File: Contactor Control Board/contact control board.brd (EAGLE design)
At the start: 57.1 x 50.8 mm, 35 parts, among them Q1 MMBT2222A, Q2 MMBT2222A, Q3 IRLML6344TRPBF, Q6 IRLML6344TRPBF

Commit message: Routed BMS interface board and added branding.
Changed branding for CCB and MCBs
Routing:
- net CONTACT_EN: track 91.4 -> 90.1 mm
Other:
- board text added: "Prosthesis CCB V1.0"
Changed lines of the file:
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@@
 <text x="25.7175" y="6.6675" size="1.016" layer="25" font="vector" ratio="15">+ve</text>
 <text x="13.6525" y="6.6675" size="1.016" layer="25" font="vector" ratio="15">+ve</text>
+<text x="40.64" y="13.0175" size="1.778" layer="25" font="vector" ratio="15">Prosthesis
+CCB V1.0</text>
 </plain>
 <attributes>
@@
 <wire x1="20.32" y1="1.905" x2="50.4825" y2="1.905" width="0.3048" layer="1"/>
 <wire x1="50.4825" y1="1.905" x2="51.1175" y2="2.54" width="0.3048" layer="1"/>
-<wire x1="51.1175" y1="2.54" x2="51.1175" y2="13.335" width="0.3048" layer="1"/>
-<wire x1="51.1175" y1="13.335" x2="51.435" y2="13.6525" width="0.3048" layer="1"/>
-<via x="51.435" y="13.6525" extent="1-16" drill="0.508"/>
-<wire x1="51.435" y1="13.6525" x2="53.6575" y2="13.6525" width="0.3048" layer="16"/>
+<wire x1="51.1175" y1="2.54" x2="51.1175" y2="11.1125" width="0.3048" layer="1"/>
+<wire x1="51.1175" y1="11.1125" x2="53.6575" y2="13.6525" width="0.3048" layer="1"/>
+<via x="53.6575" y="13.6525" extent="1-16" drill="0.762"/>
 <wire x1="53.6575" y1="13.6525" x2="54.61" y2="14.605" width="0.3048" layer="16"/>
 <wire x1="54.61" y1="14.605" x2="54.61" y2="21.2725" width="0.3048" layer="16"/>

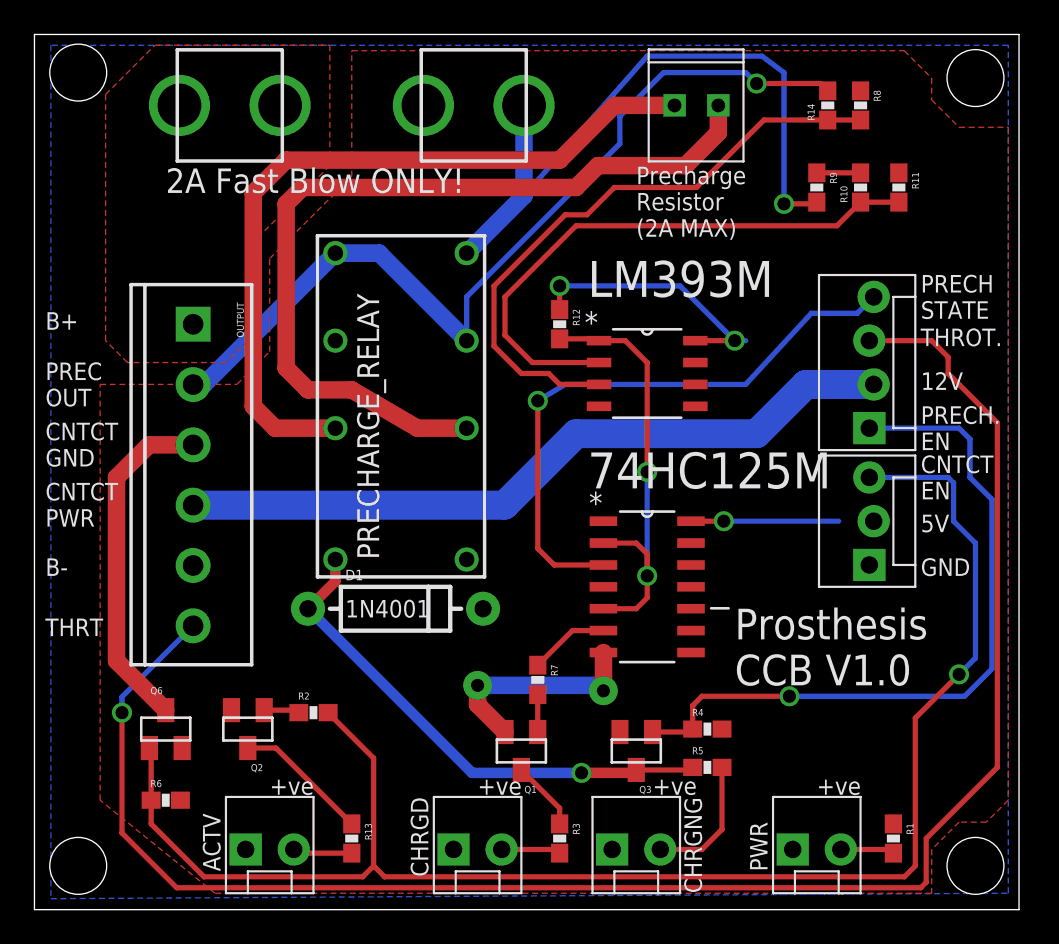
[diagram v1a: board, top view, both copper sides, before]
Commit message: UPdating resistor packages to sizes which are
capable of disappating the appropriate amount of power.
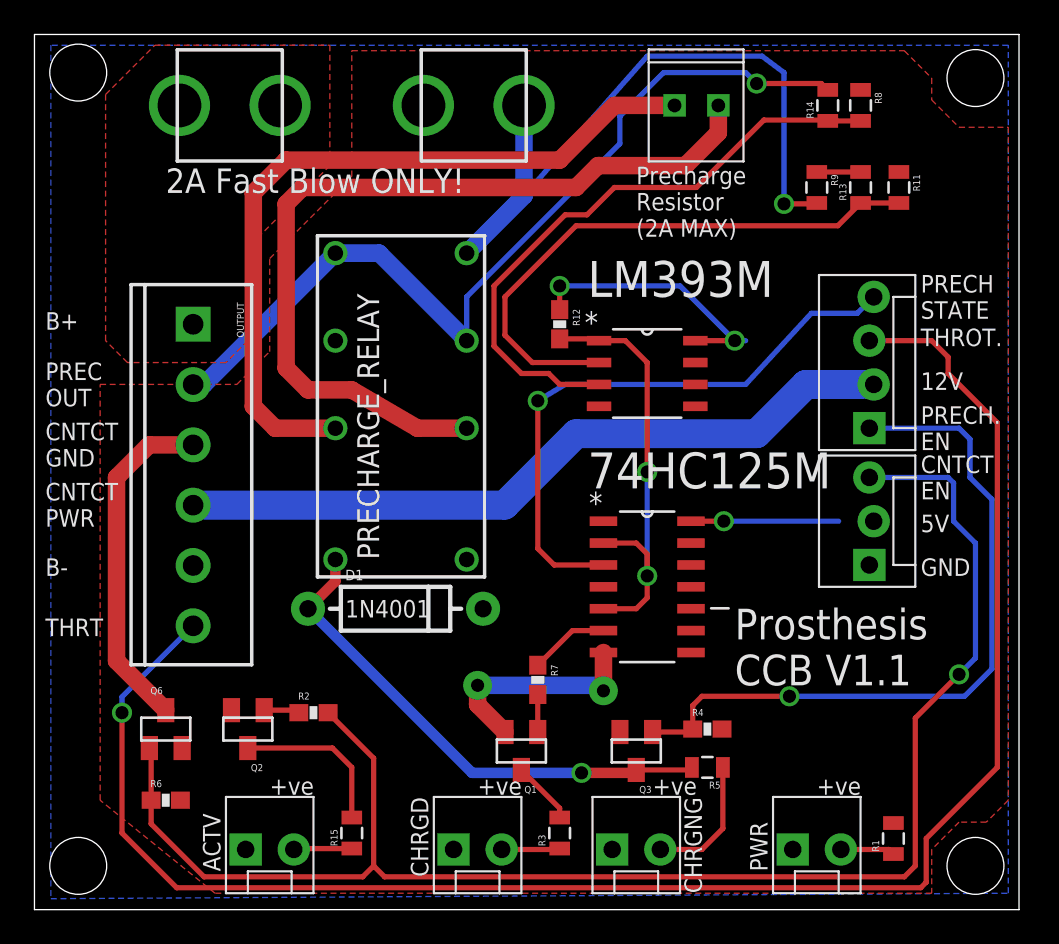
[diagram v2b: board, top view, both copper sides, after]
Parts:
- removed R10: 110k, SparkFun-Resistors:0603-RES
- added R15: 470, SparkFun-Resistors:0805
- R1, R14, R3, R5, R9: device SparkFun-Resistors:0603-RES -> SparkFun-Resistors:0805
- R11: value 12k -> 12K; device SparkFun-Resistors:0603-RES -> SparkFun-Resistors:0805
- R13: value 470 -> 110k; device SparkFun-Resistors:0603-RES -> SparkFun-Resistors:0805
- R8: value 13k -> 13K; device SparkFun-Resistors:0603-RES -> SparkFun-Resistors:0805
- moved R13 48.0 mm to (47.9, 41.9), turned to 90 degrees
- moved R3 0.32 mm to (30.5, 4.45), turned to 90 degrees
- turned R1 to 90 degrees
- turned R5 to 180 degrees
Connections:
- net CAP_CHARGE_REF: now also R13.1; no longer R10.1
- net GND: now also R1.2; no longer R1.1
- net N$1: now also R15.2; no longer R13.1
- net N$12: now also R1.1; no longer R1.2
- net N$3: now also R13.2; no longer R10.2
- net N$4: now also R3.1; no longer R3.2
- net N$5: now also R3.2; no longer R3.1
- net N$7: now also R5.1; no longer R5.2
- net N$9: now also R15.1; no longer R13.2
- net PRECH_DRAIN: now also R5.2; no longer R5.1
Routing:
- net N$1: track 7.86 -> 9.41 mm
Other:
- board text added: "Prosthesis CCB V1.1"
- board text removed: "Prosthesis CCB V1.0"

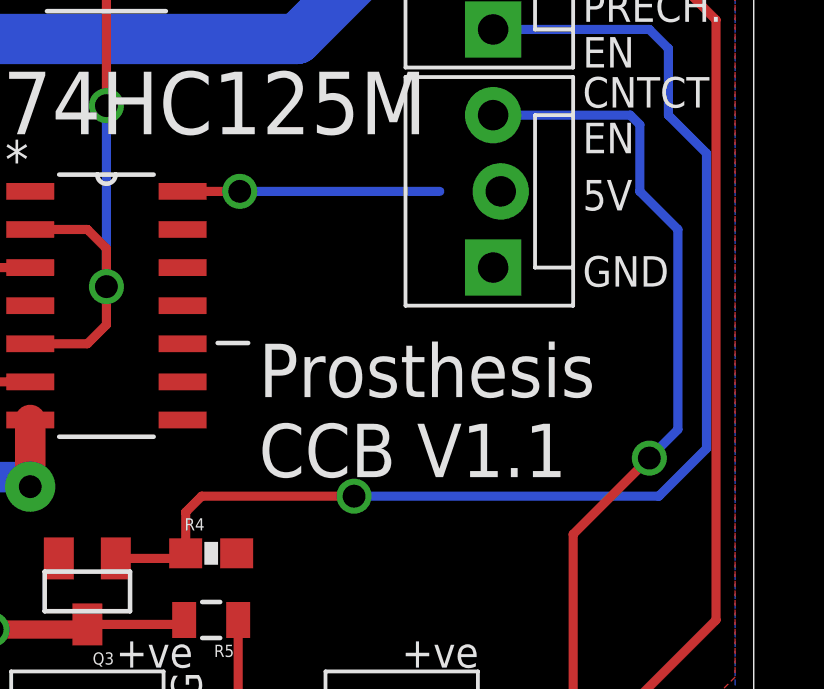
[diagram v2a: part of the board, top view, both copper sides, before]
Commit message: Added capacitors for the three main boards
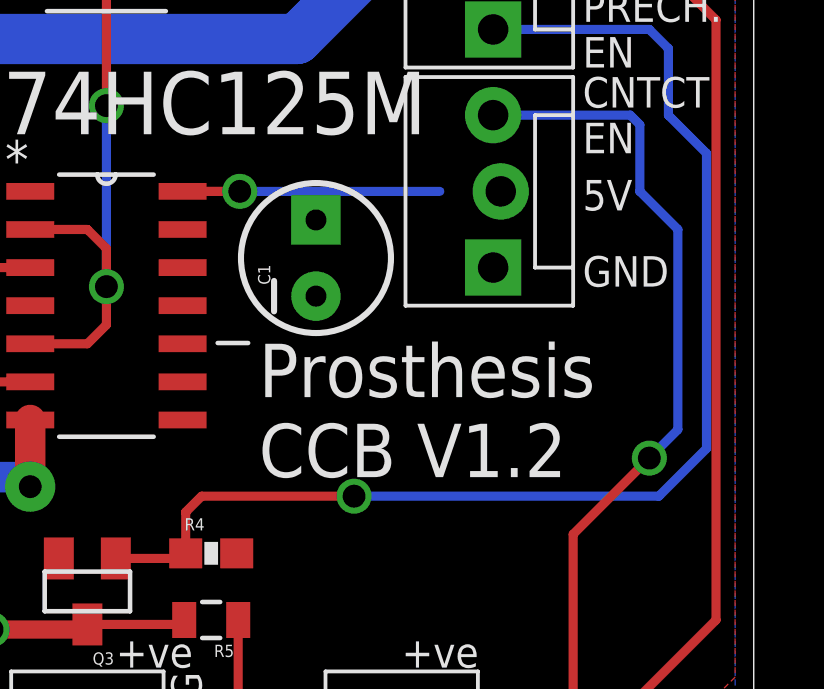
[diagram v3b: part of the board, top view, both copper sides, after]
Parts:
- added C1: 10uF, SparkFun-Capacitors:CPOL-RADIAL-10UF-25V
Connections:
- net 5V: now also C1.1
- net GND: now also C1.2
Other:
- board text added: "Prosthesis CCB V1.2"
- board text removed: "Prosthesis CCB V1.1"
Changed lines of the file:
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@@
 <text x="13.6525" y="6.6675" size="1.016" layer="25" font="vector" ratio="15">+ve</text>
 <text x="40.64" y="13.0175" size="1.778" layer="25" font="vector" ratio="15">Prosthesis
-CCB V1.1</text>
+CCB V1.2</text>
 </plain>
 <attributes>
@@
 <element name="R13" library="SparkFun-Resistors" package="0805" value="110k" x="47.9425" y="41.91" rot="R90"/>
 <element name="R11" library="SparkFun-Resistors" package="0805" value="12K" x="50.165" y="41.91" rot="R270"/>
+<element name="C1" library="SparkFun-Capacitors" package="CPOL-RADIAL-10UF-25V" value="10uF" x="42.545" y="20.32" rot="R90"/>
 </elements>
 <signals>
@@
 <contactref element="PWR" pad="1"/>
 <contactref element="CHARGING" pad="1"/>
+<contactref element="C1" pad="1"/>
 </signal>
 <signal name="GND">
@@
 <contactref element="R8" pad="1"/>
 <contactref element="R11" pad="1"/>
+<contactref element="C1" pad="2"/>
 </signal>
 <signal name="CONTACT_EN">
